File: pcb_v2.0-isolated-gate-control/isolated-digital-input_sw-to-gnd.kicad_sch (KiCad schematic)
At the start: 7 parts, among them SW2 SW_SPDT

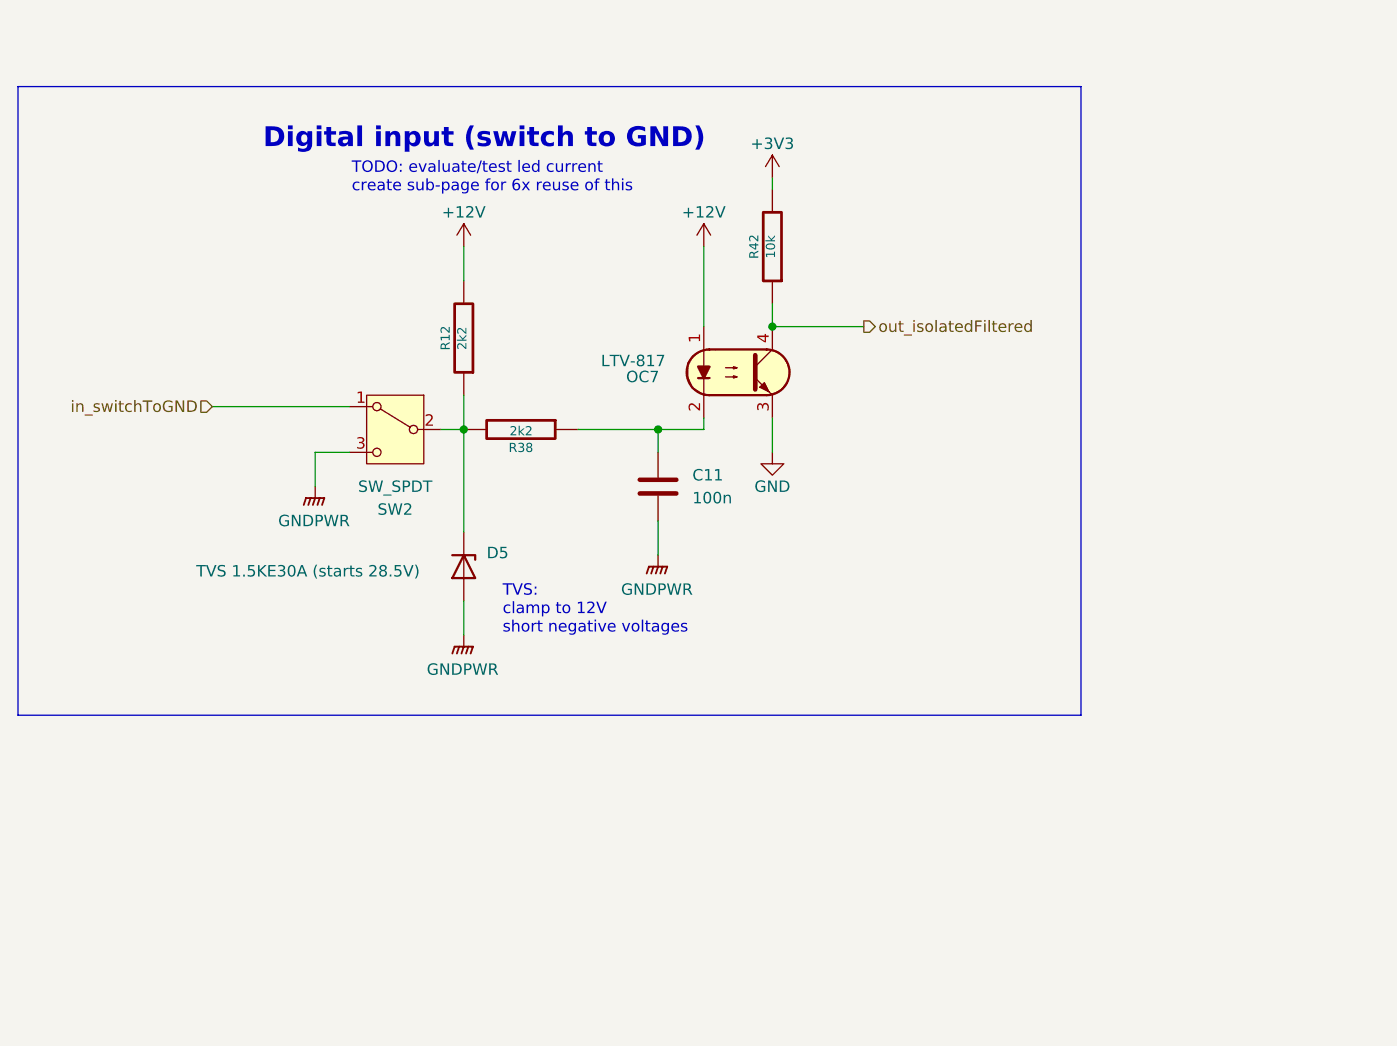
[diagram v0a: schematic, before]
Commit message: pcb: Add Relays, mosfet-out, terminals, Fix RS485 isolation
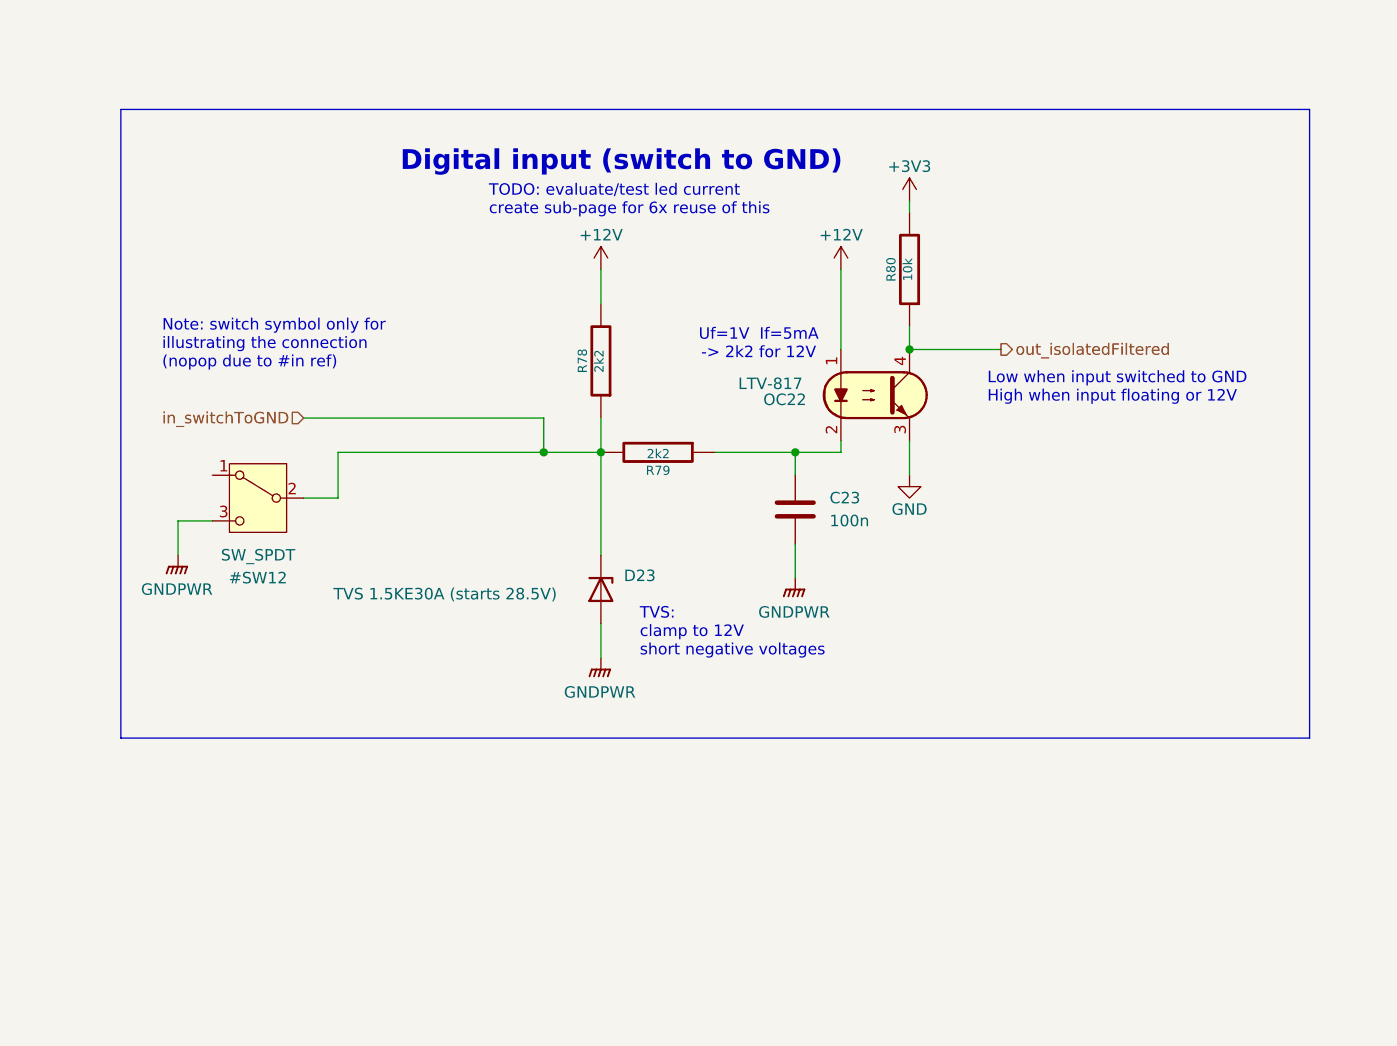
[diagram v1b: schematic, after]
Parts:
- D23: renamed from D5; footprint Diode_THT:D_DO-201AE_P15.24mm_Horizontal -> Diode_THT:D_DO-41_SOD81_P12.70mm_Horizontal
- renumbered SW2 to #SW12, C11 to C23, OC7 to OC22, R12 to R78, R38 to R79, R42 to R80
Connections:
- net in_switchToGND: now also #SW12.2 (B), D23.1 (K), R78.1, R79.2; no longer #SW12.1 (A)
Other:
- note added: "Low when input switched to GND High when input floating or 12V"
- note added: "Note: switch symbol only for illustrating the connection (nopop due to #in ref)"
- note added: "Uf=1V If=5mA -> 2k2 for 12V"
- moved on the sheet: C23, D23, OC22, R78, R79, R80

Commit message: pcb: change footprints + arrange groups individually for saving space
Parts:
- R80: footprint Resistor_THT:R_Axial_DIN0207_L6.3mm_D2.5mm_P10.16mm_Horizontal -> Resistor_THT:R_Axial_DIN0207_L6.3mm_D2.5mm_P2.54mm_Vertical
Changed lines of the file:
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@@
 			)
 		)
-		(property "Footprint" "Resistor_THT:R_Axial_DIN0207_L6.3mm_D2.5mm_P10.16mm_Horizontal"
+		(property "Footprint" "Resistor_THT:R_Axial_DIN0207_L6.3mm_D2.5mm_P2.54mm_Vertical"
 			(at 126.238 49.53 90)
 			(effects

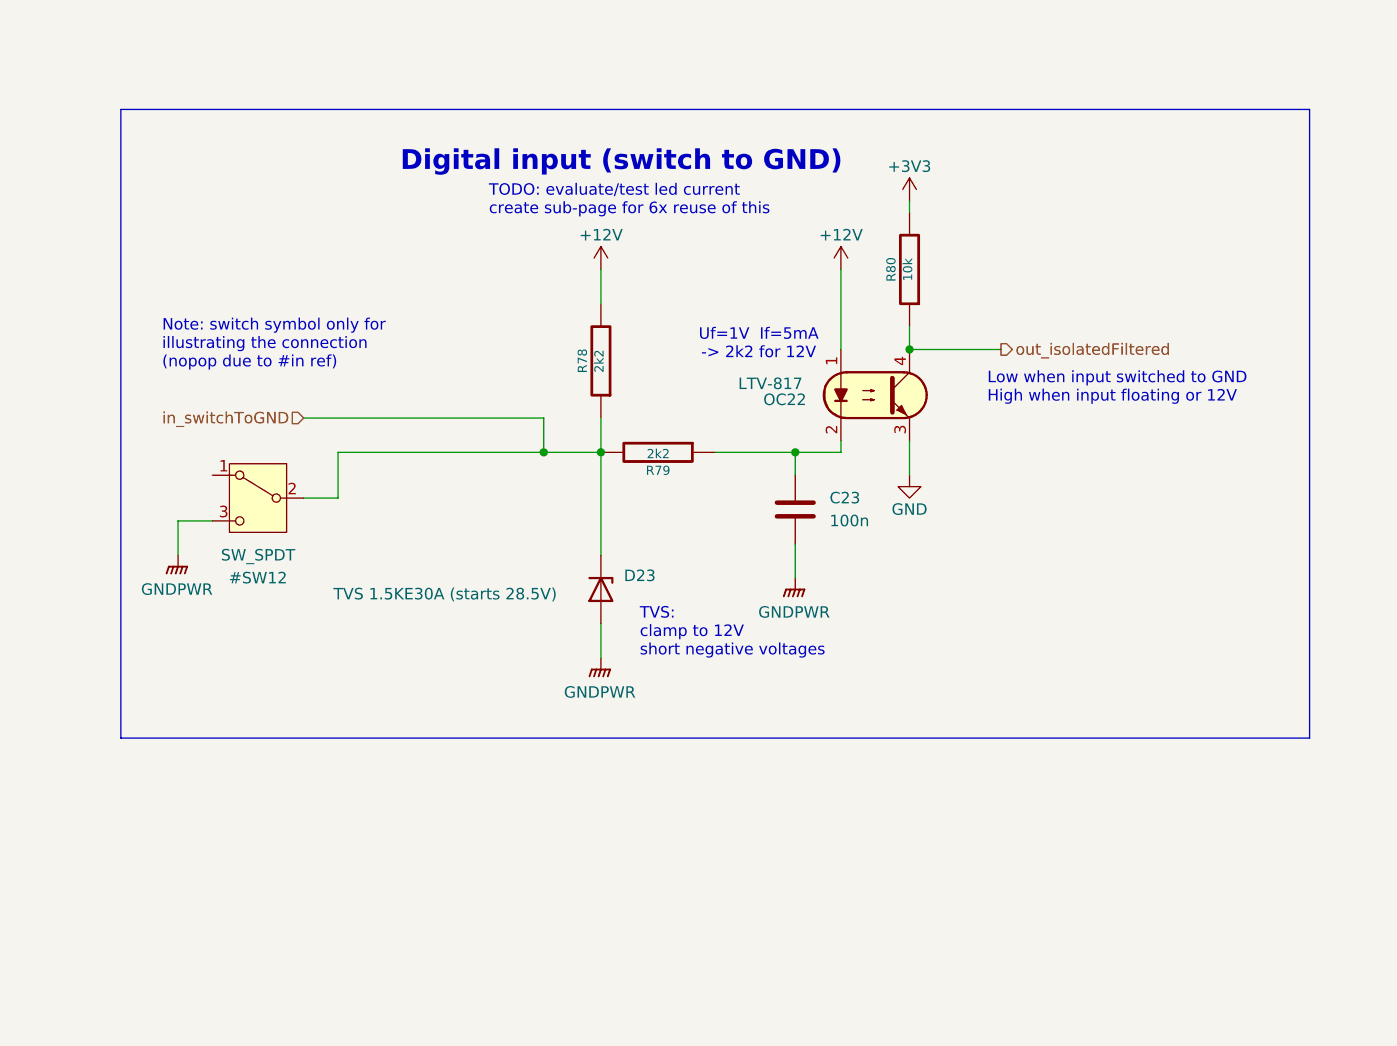
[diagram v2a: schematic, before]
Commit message: pcb: Cleanup Schematic, arrange, replace legacy-symbols, optimize for ERC pass
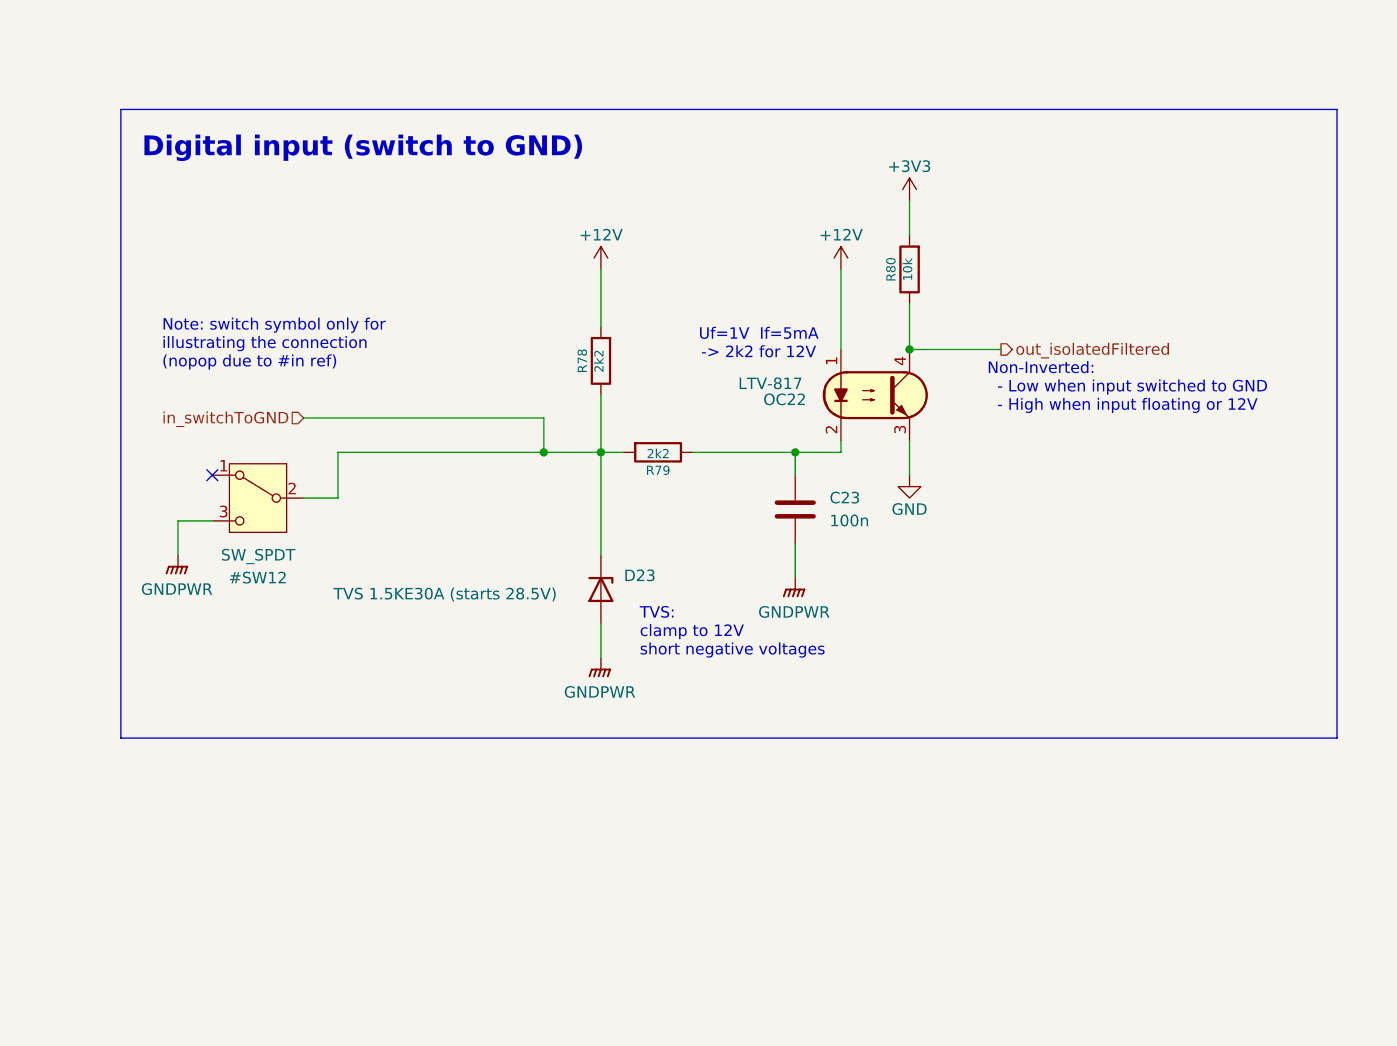
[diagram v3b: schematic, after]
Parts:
- R78, R79, R80: symbol treiber-rescue:R -> Device:R
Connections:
- no-connect marks 0 -> 1
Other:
- note added: "Non-Inverted: - Low when input switched to GND - High when input floating or 12V"
- note removed: "Low when input switched to GND High when input floating or 12V"
- note removed: "TODO: evaluate/test led current create sub-page for 6x reuse of this"
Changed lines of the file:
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@@
 		(color 0 0 0 0)
 	)
+	(no_connect
+		(at 46.99 72.39)
+	)
 	(wire
 		(pts
@@
 	(wire
 		(pts
-			(xy 90.17 49.53) (xy 90.17 53.34)
+			(xy 90.17 49.53) (xy 90.17 55.88)
 		)
 		(stroke
@@
 	(wire
 		(pts
-			(xy 90.17 66.04) (xy 90.17 69.85)
+			(xy 90.17 63.5) (xy 90.17 69.85)
 		)
 		(stroke
@@
 	(wire
 		(pts
-			(xy 102.87 69.85) (xy 111.76 69.85)
-		)
-		(stroke
-			(width 0)
-			(type default)
-		)
-	)
-	(wire
-		(pts
 			(xy 124.46 58.42) (xy 134.62 58.42)
 		)
@@
 	(wire
 		(pts
-			(xy 124.46 55.88) (xy 124.46 58.42)
+			(xy 124.46 53.34) (xy 124.46 58.42)
 		)
 		(stroke
@@
 	(wire
 		(pts
+			(xy 100.33 69.85) (xy 111.76 69.85)
+		)
+		(stroke
+			(width 0)
+			(type default)
+		)
+	)
+	(wire
+		(pts
 			(xy 111.76 69.85) (xy 111.76 72.39)
 		)
@@
 	(wire
 		(pts
-			(xy 124.46 41.91) (xy 124.46 43.18)
+			(xy 90.17 69.85) (xy 92.71 69.85)
+		)
+		(stroke
+			(width 0)
+			(type default)
+		)
+	)
+	(wire
+		(pts
+			(xy 124.46 41.91) (xy 124.46 45.72)
 		)
 		(stroke
@@
 	(rectangle
 		(start 36.83 31.75)
-		(end 168.91 101.6)
+		(end 171.958 101.6)
 		(stroke
 			(width 0)
@@
 	(text "Digital input (switch to GND)"
 		(exclude_from_sim no)
-		(at 92.456 37.592 0)
+		(at 63.754 36.068 0)
 		(effects
 			(font
@@
 		)
 	)
-	(text "Low when input switched to GND\nHigh when input floating or 12V"
+	(text "Non-Inverted:\n  - Low when input switched to GND\n  - High when input floating or 12V"
 		(exclude_from_sim no)
 		(at 133.096 62.738 0)
-		(effects
-			(font
-				(size 1.27 1.27)
-			)
-			(justify left)
-		)
-	)
-	(text "TODO: evaluate/test led current\ncreate sub-page for 6x reuse of this"
-		(exclude_from_sim no)
-		(at 77.724 41.91 0)
 		(effects
 			(font
@@
 	)
 	(symbol
-		(lib_id "treiber-rescue:R")
+		(lib_id "Device:R")
 		(at 124.46 49.53 180)
 		(unit 1)
@@
 			(effects
 				(font
-					(size 0.762 0.762)
-				)
-			)
-		)
-		(property "Description" ""
+					(size 1.27 1.27)
+				)
+				(hide yes)
+			)
+		)
+		(property "Description" "Resistor"
 			(at 124.46 49.53 0)
 			(effects
@@
 	)
 	(symbol
-		(lib_id "treiber-rescue:R")
+		(lib_id "Device:R")
 		(at 90.17 59.69 180)
 		(unit 1)
@@
 			(effects
 				(font
-					(size 0.762 0.762)
-				)
-			)
-		)
-		(property "Description" ""
+					(size 1.27 1.27)
+				)
+				(hide yes)
+			)
+		)
+		(property "Description" "Resistor"
 			(at 90.17 59.69 0)
 			(effects
@@
 	)
 	(symbol
-		(lib_id "treiber-rescue:R")
+		(lib_id "Device:R")
 		(at 96.52 69.85 270)
 		(unit 1)
@@
 			(effects
 				(font
-					(size 0.762 0.762)
-				)
-			)
-		)
-		(property "Description" ""
+					(size 1.27 1.27)
+				)
+				(hide yes)
+			)
+		)
+		(property "Description" "Resistor"
 			(at 96.52 69.85 0)
 			(effects

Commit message: pcb: finish todos, Fix esp32 power issues, document tests, dualType C footprint
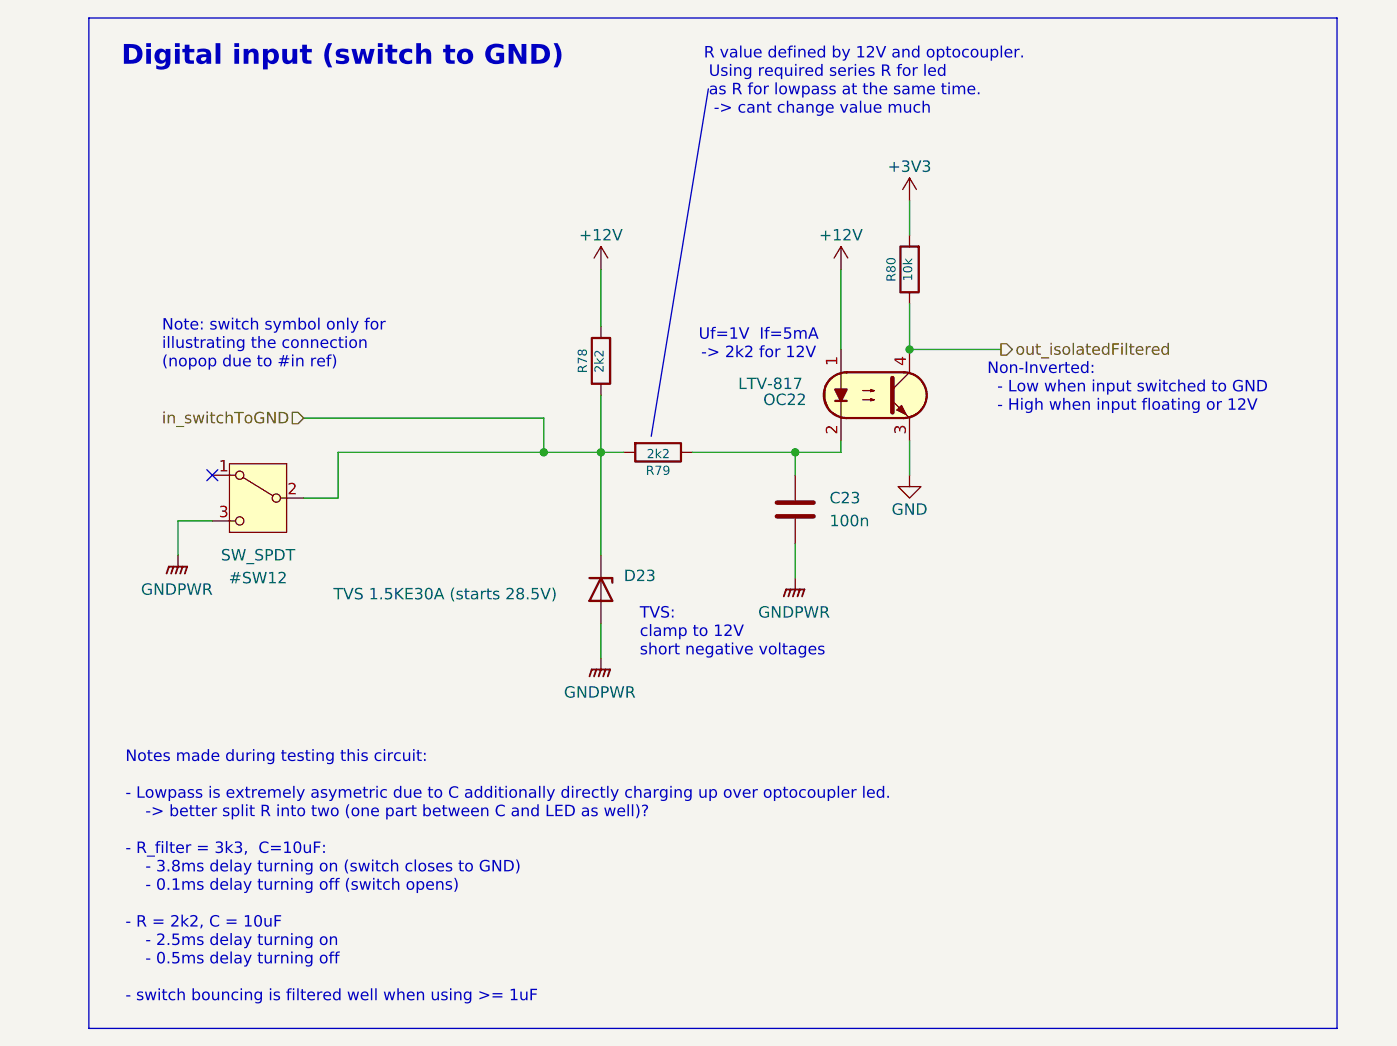
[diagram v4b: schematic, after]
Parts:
- C23: footprint Capacitor_THT:C_Disc_D7.0mm_W2.5mm_P5.00mm -> capacitor_libJonny:C_DualType__Disc-7.0x2.5mm-P5mm__Elko-D5mm-P2.5mm
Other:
- note added: "Notes made during testing this circuit: - Lowpass is extremely asymetric due to C additionally directly charging up over optocoupler led. -> better split R into two (one part between C and LED as well)? - R_filter = 3k3, C=10uF: - 3.8ms delay turning on (switch closes to GND) - 0.1ms delay turning off (switch opens) - R = 2k2, C = 10uF - 2.5ms delay turning on - 0.5ms delay turning off - switch b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"
- note added: "R value defined by 12V and optocoupler. Using required series R for led as R for lowpass at the same time. -> cant change value much"
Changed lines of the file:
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@@
+		)
+	)
+	(polyline
+		(pts
+			(xy 102.108 29.464) (xy 95.758 68.072)
+		)
+		(stroke
+			(width 0)
+			(type default)
 		)
 	)
@@
 	)
 	(rectangle
-		(start 36.83 31.75)
-		(end 171.958 101.6)
+		(start 33.274 21.59)
+		(end 171.958 133.858)
 		(stroke
 			(width 0)
@@
 		)
 	)
+	(text "R value defined by 12V and optocoupler.\n Using required series R for led\n as R for lowpass at the same time.\n  -> cant change value much"
+		(exclude_from_sim no)
+		(at 101.6 28.702 0)
+		(effects
+			(font
+				(size 1.27 1.27)
+			)
+			(justify left)
+		)
+	)
 	(text "TVS:\nclamp to 12V\nshort negative voltages"
 		(exclude_from_sim no)
@@
 	(text "Digital input (switch to GND)"
 		(exclude_from_sim no)
-		(at 63.754 36.068 0)
+		(at 61.468 25.908 0)
 		(effects
 			(font
@@
 		(exclude_from_sim no)
 		(at 133.096 62.738 0)
+		(effects
+			(font
+				(size 1.27 1.27)
+			)
+			(justify left)
+		)
+	)
+	(text "Notes made during testing this circuit:\n\n- Lowpass is extremely asymetric due to C additionally directly charging up over optocoupler led.\n	-> better split R into two (one part between C and LED as well)?\n\n- R_filter = 3k3,  C=10uF:\n	- 3.8ms delay turning on (switch closes to GND)\n	- 0.1ms delay turning off (switch opens)\n\n- R = 2k2, C = 10uF\n	- 2.5ms delay turning on\n	- 0.5ms delay turning off\n\n- switch bouncing is filtered well when using >= 1uF"
+		(exclude_from_sim no)
+		(at 37.338 117.094 0)
 		(effects
 			(font
@@
 			)
 		)
-		(property "Footprint" "Capacitor_THT:C_Disc_D7.0mm_W2.5mm_P5.00mm"
+		(property "Footprint" "capacitor_libJonny:C_DualType__Disc-7.0x2.5mm-P5mm__Elko-D5mm-P2.5mm"
 			(at 112.7252 80.01 0)
 			(effects
